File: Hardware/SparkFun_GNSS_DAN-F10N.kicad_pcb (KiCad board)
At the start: 4 copper layers, 40.6 x 40.6 mm, 91 parts, among them J1 USB_C_Receptacle, J2 Conn_01x06, J4 U.FL, J5 Conn_01x09, U1 DT1042-04SO, U3 RT9080-3.3, U4 CH340C, U5 DAN-F10N

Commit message: Add ignore
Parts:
- added kibuzzard-67D3586F: G***, kibuzzard-67D3586F, B.Cu at (159.4, 114.3)
- added kibuzzard-67D35894: G***, kibuzzard-67D35894, B.Cu at (156.8, 114.3)
- added kibuzzard-67D3589A: G***, kibuzzard-67D3589A, B.Cu at (154.3, 114.1)
- added kibuzzard-67D358AB: G***, kibuzzard-67D358AB, B.Cu at (149.2, 114.1)
- moved G*** 0.79 mm to (155.6, 84.8)
- moved kibuzzard-67C52A06 0.64 mm to (155.6, 111.1)
- moved kibuzzard-67C529FB 0.32 mm to (155.6, 108.9)

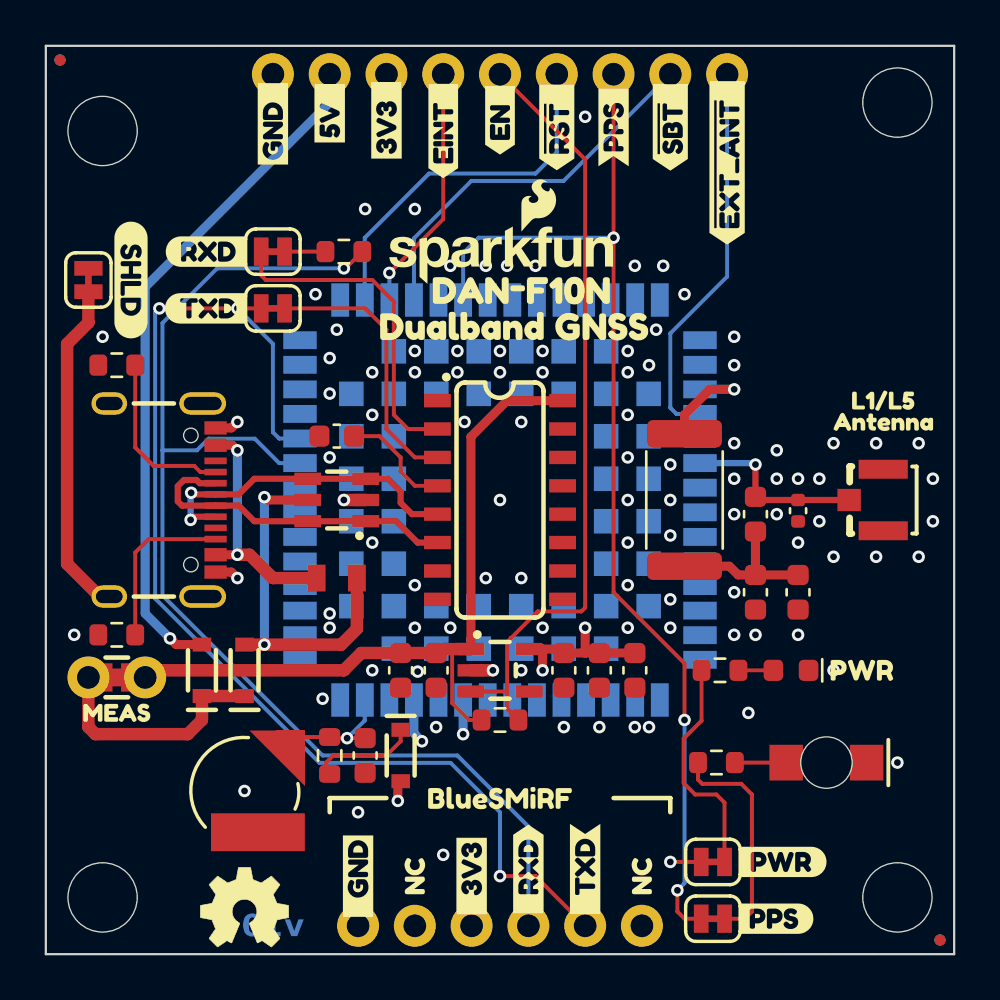
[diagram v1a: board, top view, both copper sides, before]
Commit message: Fix DAN-F10N footprint. Move EXT_ANT to jumper.
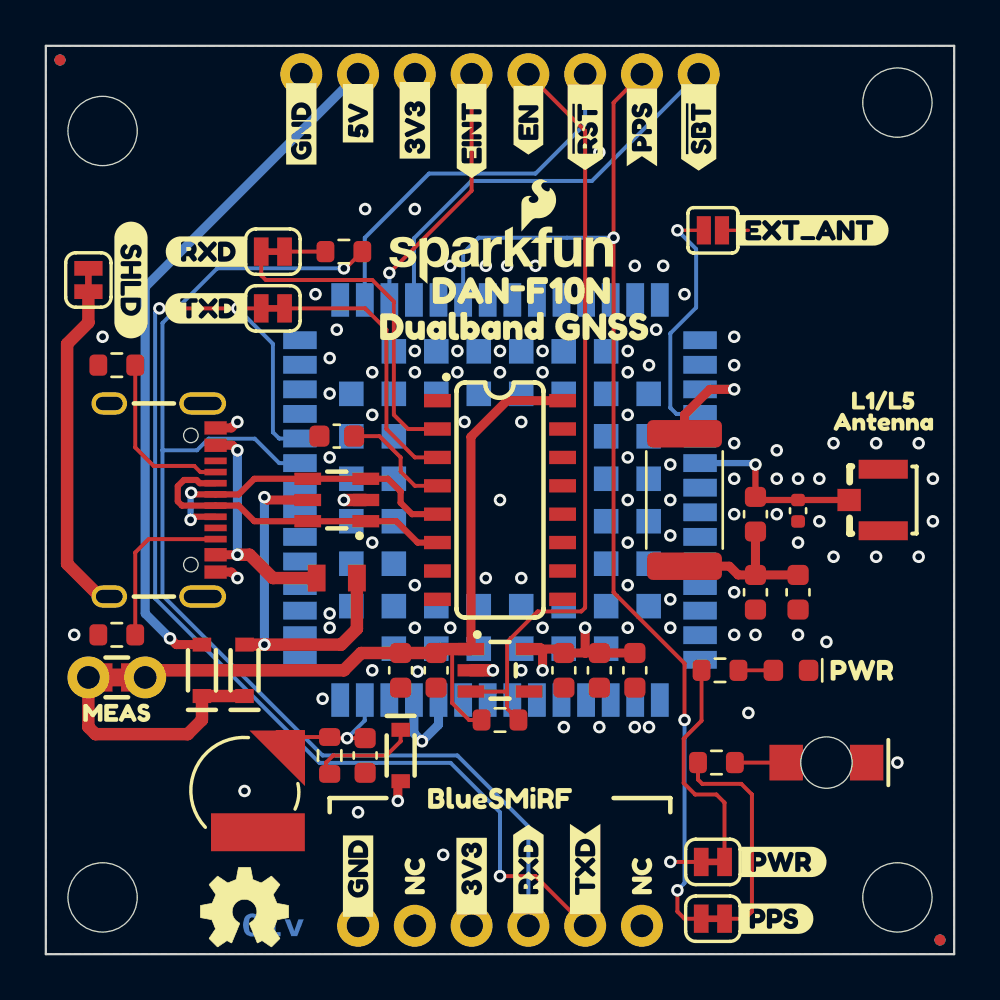
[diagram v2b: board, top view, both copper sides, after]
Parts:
- removed kibuzzard-67D338F1: G***, kibuzzard-67D338F1
- removed kibuzzard-67D338FB: G***, kibuzzard-67D338FB
- added JP1: EXT_ANT, SparkFun-Jumper:Jumper_2_NO, F.Cu at (165.1, 85.1)
- added kibuzzard-67EB0CBA: G***, kibuzzard-67EB0CBA, F.Cu at (169.5, 85.1)
- J5: value Conn_01x09 -> Conn_01x08; footprint SparkFun-Connector:1x09 -> SparkFun-Connector:1x08
- R5: value 1k -> 330
- U5: footprint Hardware:DAN-F10N -> SparkFun_GNSS_LG580P:DAN-F10N
- moved J5 1.27 mm to (164.5, 78.1)
- moved kibuzzard-67C52692 1.27 mm to (156.8, 80.2)
- moved kibuzzard-67C526C1 1.27 mm to (161.9, 80.5)
- moved kibuzzard-67C526DE 1.27 mm to (164.5, 80.5)
- moved kibuzzard-67C526ED 1.27 mm to (154.3, 80.6)
- moved kibuzzard-67C52701 1.27 mm to (146.7, 80.3)
- moved kibuzzard-67C52734 1.27 mm to (146.7, 80.3)
- moved kibuzzard-67C5274E 1.27 mm to (154.3, 80.6)
- moved kibuzzard-67C5275D 1.27 mm to (156.8, 80.2)
- moved kibuzzard-67C52789 1.27 mm to (161.9, 80.3)
- moved kibuzzard-67C5279A 1.27 mm to (164.5, 80.5)
- moved kibuzzard-67C526AF 1.27 mm to (159.4, 80.5)
- moved kibuzzard-67C526F3 1.27 mm to (151.8, 80.2)
- moved kibuzzard-67C526FD 1.27 mm to (149.2, 79.9)
- moved kibuzzard-67C52738 1.27 mm to (149.2, 79.9)
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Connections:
- J5 pad 1: ~{EXT_ANT} -> ~{SAFEBOOT}
- J5 pad 2: ~{SAFEBOOT} -> PPS
- J5 pad 3: PPS -> ~{RESET}
- J5 pad 4: ~{RESET} -> 3V3_EN
- J5 pad 5: 3V3_EN -> EXTINT
- J5 pad 6: EXTINT -> 3.3V
- J5 pad 7: 3.3V -> 5V
- J5 pad 8: 5V -> GND
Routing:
- net ~{EXT_ANT}: track 17.4 -> 11.4 mm, vias 0 -> 1
- net ~{SAFEBOOT}: track 17.3 -> 18.5 mm
- net GND: track 4.14 -> 5.33 mm, vias 97 -> 96
- net 3.3V: track 12.7 -> 13.3 mm, vias 6 -> 5
- net EXTINT: track 11.1 -> 11.6 mm
- net PPS: track 49.2 -> 49.7 mm
- net 3V3_EN: track 34.9 -> 34.4 mm
- net ~{RESET}: track 16.4 -> 17.0 mm
- net 5V: track 30.7 -> 31.2 mm

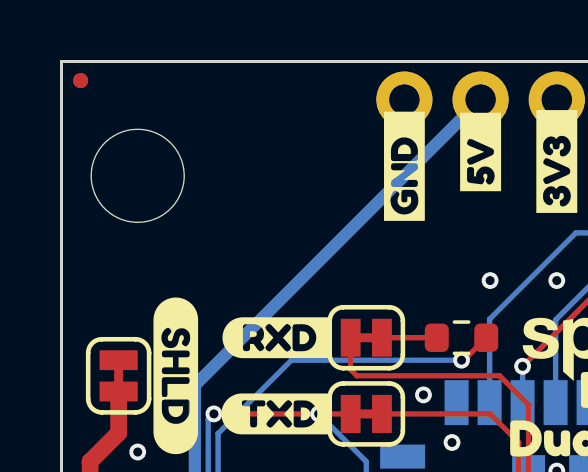
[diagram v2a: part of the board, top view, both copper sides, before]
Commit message: Fix standoff location. Update to v9.
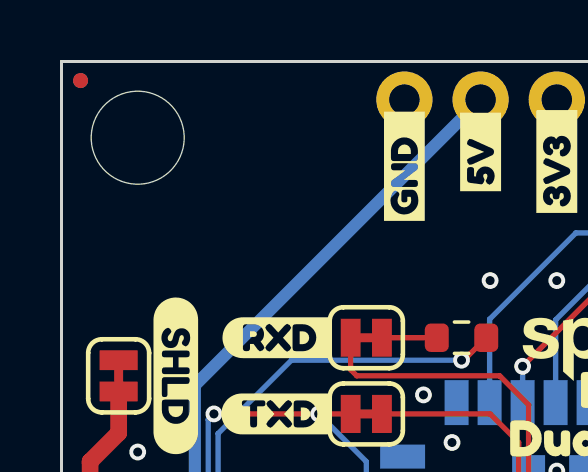
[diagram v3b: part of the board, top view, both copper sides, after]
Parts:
- moved ST3 1.27 mm to (137.8, 79.4)

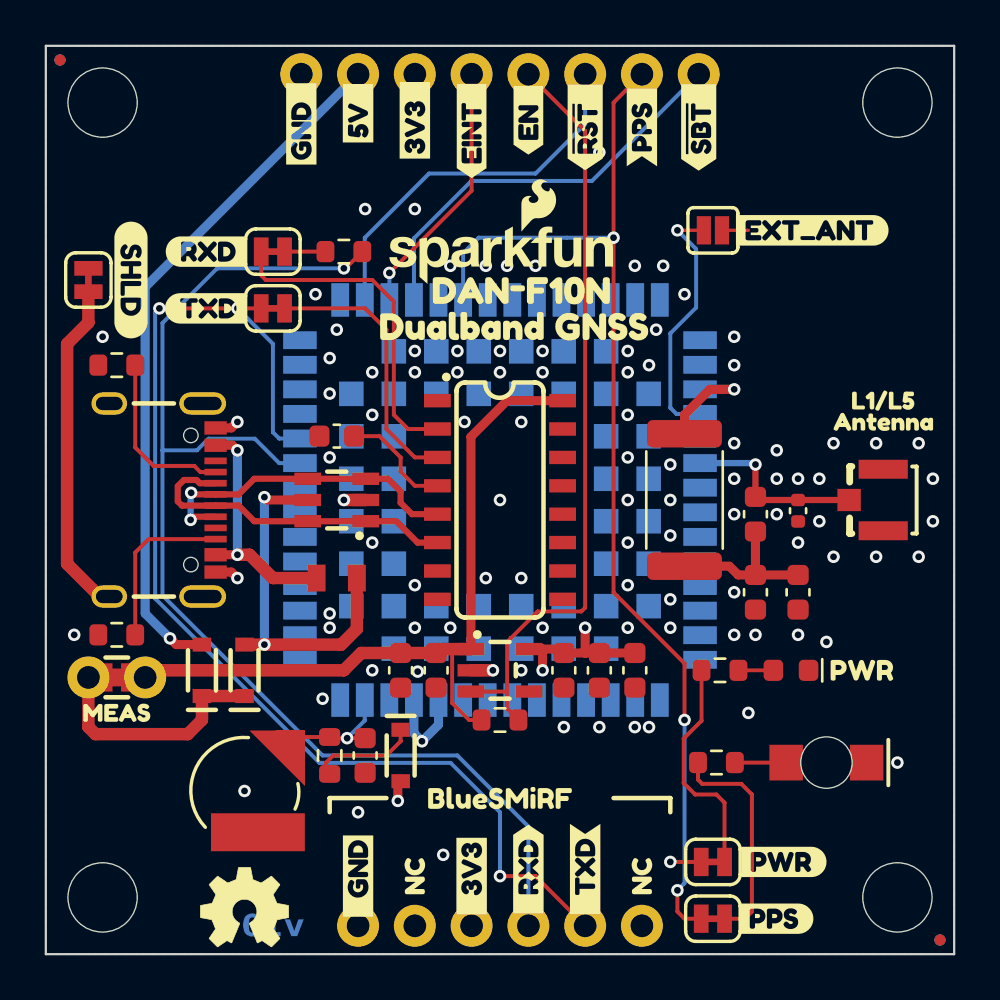
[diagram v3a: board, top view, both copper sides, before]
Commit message: Reduce paste on signal pads. Correct EXT_ANT activation level.
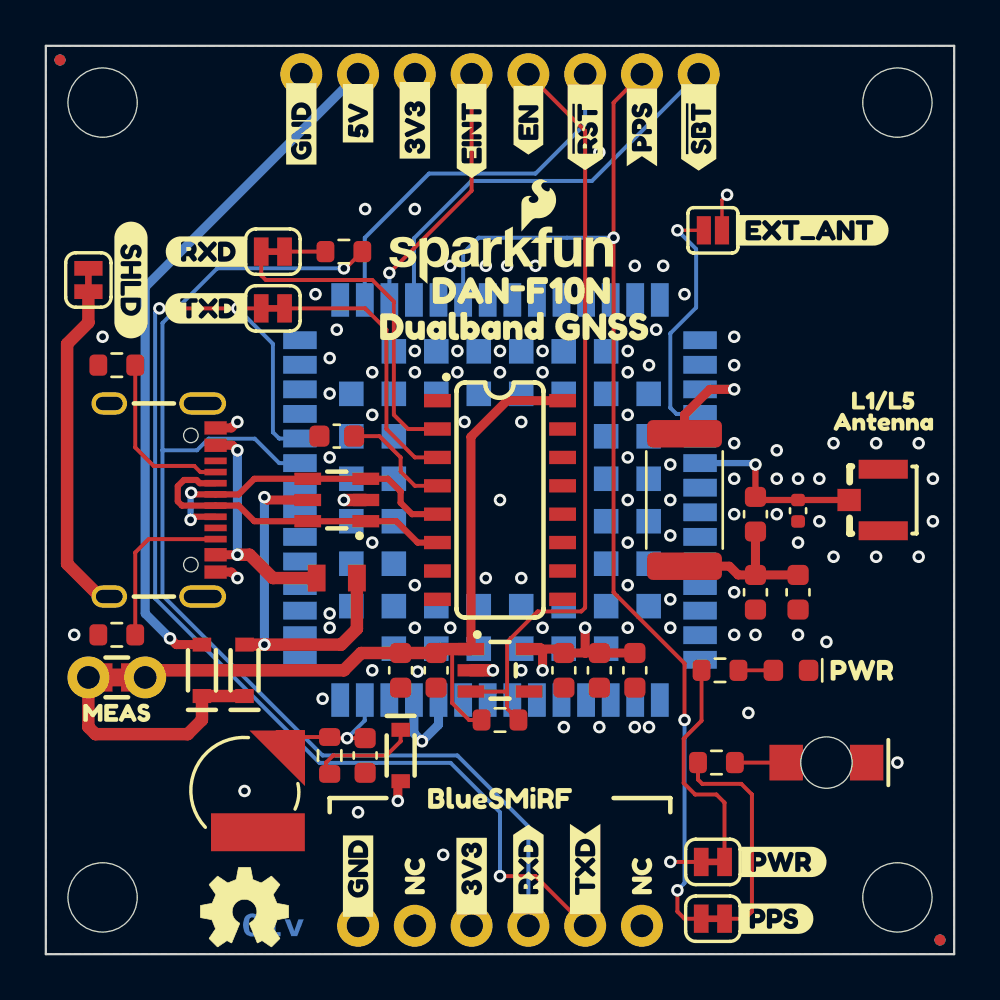
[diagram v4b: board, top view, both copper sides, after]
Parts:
- removed U5: DAN-F10N, SparkFun_GNSS_LG580P:DAN-F10N
- added U6: DAN-F10N, DAN-F10N:DAN-F10N, B.Cu at (155.6, 97.2)
- kibuzzard-64C2E6A3: footprint kibuzzard-64C2E6A3 -> DAN-F10N:kibuzzard-64C2E6A3
- kibuzzard-64C3DF93: footprint kibuzzard-64C3DF93 -> DAN-F10N:kibuzzard-64C3DF93
- kibuzzard-6501FDDA: footprint kibuzzard-6501FDDA -> DAN-F10N:kibuzzard-6501FDDA
- kibuzzard-67C524B9: footprint kibuzzard-67C524B9 -> DAN-F10N:kibuzzard-67C524B9
- kibuzzard-67C524C4: footprint kibuzzard-67C524C4 -> DAN-F10N:kibuzzard-67C524C4
- kibuzzard-67C52692: footprint kibuzzard-67C52692 -> DAN-F10N:kibuzzard-67C52692
- kibuzzard-67C526AF: footprint kibuzzard-67C526AF -> DAN-F10N:kibuzzard-67C526AF
- kibuzzard-67C526C1: footprint kibuzzard-67C526C1 -> DAN-F10N:kibuzzard-67C526C1
- kibuzzard-67C526DE: footprint kibuzzard-67C526DE -> DAN-F10N:kibuzzard-67C526DE
- kibuzzard-67C526ED: footprint kibuzzard-67C526ED -> DAN-F10N:kibuzzard-67C526ED
- kibuzzard-67C526F3: footprint kibuzzard-67C526F3 -> DAN-F10N:kibuzzard-67C526F3
- kibuzzard-67C526FD: footprint kibuzzard-67C526FD -> DAN-F10N:kibuzzard-67C526FD
- kibuzzard-67C52701: footprint kibuzzard-67C52701 -> DAN-F10N:kibuzzard-67C52701
- kibuzzard-67C52734: footprint kibuzzard-67C52734 -> DAN-F10N:kibuzzard-67C52734
- kibuzzard-67C52738: footprint kibuzzard-67C52738 -> DAN-F10N:kibuzzard-67C52738
- kibuzzard-67C5273C: footprint kibuzzard-67C5273C -> DAN-F10N:kibuzzard-67C5273C
- kibuzzard-67C5274E: footprint kibuzzard-67C5274E -> DAN-F10N:kibuzzard-67C5274E
- kibuzzard-67C5275D: footprint kibuzzard-67C5275D -> DAN-F10N:kibuzzard-67C5275D
- kibuzzard-67C52789: footprint kibuzzard-67C52789 -> DAN-F10N:kibuzzard-67C52789
- kibuzzard-67C5279A: footprint kibuzzard-67C5279A -> DAN-F10N:kibuzzard-67C5279A
- kibuzzard-67C527CA: footprint kibuzzard-67C527CA -> DAN-F10N:kibuzzard-67C527CA
- kibuzzard-67C529FB: footprint kibuzzard-67C529FB -> DAN-F10N:kibuzzard-67C529FB
- kibuzzard-67C52A06: footprint kibuzzard-67C52A06 -> DAN-F10N:kibuzzard-67C52A06
- kibuzzard-67C52AED: footprint kibuzzard-67C52AED -> DAN-F10N:kibuzzard-67C52AED
- kibuzzard-67C52B01: footprint kibuzzard-67C52B01 -> DAN-F10N:kibuzzard-67C52B01
- kibuzzard-67C52B1C: footprint kibuzzard-67C52B1C -> DAN-F10N:kibuzzard-67C52B1C
- kibuzzard-67C52C8F: footprint kibuzzard-67C52C8F -> DAN-F10N:kibuzzard-67C52C8F
- kibuzzard-67C52CCE: footprint kibuzzard-67C52CCE -> DAN-F10N:kibuzzard-67C52CCE
- kibuzzard-67C52D79: footprint kibuzzard-67C52D79 -> DAN-F10N:kibuzzard-67C52D79
- kibuzzard-67C52D85: footprint kibuzzard-67C52D85 -> DAN-F10N:kibuzzard-67C52D85
- kibuzzard-67C52DD7: footprint kibuzzard-67C52DD7 -> DAN-F10N:kibuzzard-67C52DD7
- kibuzzard-67C52DE1: footprint kibuzzard-67C52DE1 -> DAN-F10N:kibuzzard-67C52DE1
- kibuzzard-67C52F63: footprint kibuzzard-67C52F63 -> DAN-F10N:kibuzzard-67C52F63
- kibuzzard-67C7D061: footprint kibuzzard-67C7D061 -> DAN-F10N:kibuzzard-67C7D061
- kibuzzard-67C7D06A: footprint kibuzzard-67C7D06A -> DAN-F10N:kibuzzard-67C7D06A
- kibuzzard-67D33FB6 (x2): footprint kibuzzard-67D33FB6 -> DAN-F10N:kibuzzard-67D33FB6
- kibuzzard-67D3586F: footprint kibuzzard-67D3586F -> DAN-F10N:kibuzzard-67D3586F
- kibuzzard-67D35894: footprint kibuzzard-67D35894 -> DAN-F10N:kibuzzard-67D35894
- kibuzzard-67D3589A: footprint kibuzzard-67D3589A -> DAN-F10N:kibuzzard-67D3589A
- kibuzzard-67D358AB: footprint kibuzzard-67D358AB -> DAN-F10N:kibuzzard-67D358AB
- kibuzzard-67EB0CBA: footprint kibuzzard-67EB0CBA -> DAN-F10N:kibuzzard-67EB0CBA
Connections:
- JP1 pad 1: GND -> 3.3V
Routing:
- net 3.3V: track 13.3 -> 15.0 mm, vias 5 -> 6
- net GND: track 5.33 -> 4.14 mm

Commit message: Add panel
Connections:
- net ~{EXT_ANT} renamed EXT_ANT
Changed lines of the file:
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@@
 	(net 42 "RXD")
 	(net 43 "TXD")
-	(net 44 "~{EXT_ANT}")
+	(net 44 "EXT_ANT")
 	(net 45 "Net-(C1-Pad1)")
 	(net 46 "VDD")
@@
 			(size 0.635 1.27)
 			(layers "F.Cu" "F.Mask")
-			(net 44 "~{EXT_ANT}")
+			(net 44 "EXT_ANT")
 			(pinfunction "B")
 			(pintype "passive")
@@
 			(size 1.5 0.8)
 			(layers "B.Cu" "B.Mask" "B.Paste")
-			(net 44 "~{EXT_ANT}")
+			(net 44 "EXT_ANT")
 			(pinfunction "ANT_CTRL")
 			(pintype "input")

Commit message: Update PCB details
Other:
- board text added: "Controlled Impedance: JLC04161H-7628"
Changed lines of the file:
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@@
+		)
+	)
+	(gr_text "Controlled Impedance: JLC04161H-7628"
+		(at 236.22 171.7675 0)
+		(layer "Eco1.User")
+		(effects
+			(font
+				(size 1.27 1.27)
+				(thickness 0.15)
+			)
+			(justify left bottom)
 		)
 	)

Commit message: Remove local FP/SYM. Update to main kicad library.
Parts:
- J4: value U.FL -> Val**
- U6: footprint DAN-F10N:DAN-F10N -> SparkFun-GNSS:u-blox_DAN-F10N
